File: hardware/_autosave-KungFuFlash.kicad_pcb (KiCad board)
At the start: 2 copper layers, 62 x 83.6 mm, 46 parts, among them J1 USB Power, J2 USB_B_Mini, J4 SWD, Q1 BC817, SW1 Reset, SW2 Menu, SW3 Special, U1 C64-Exp-Port, U2 AMS1117-3.3, U3 STM32F405RGTx, Y1 8MHz

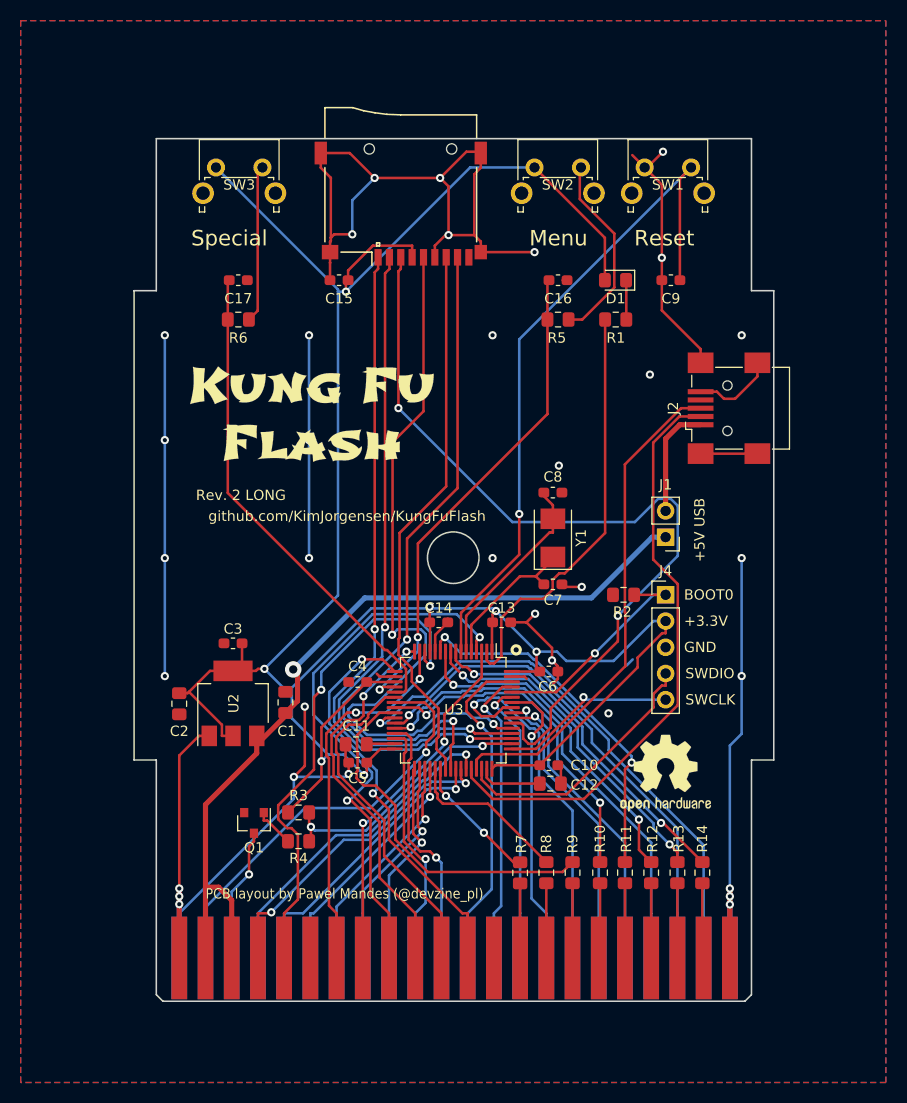
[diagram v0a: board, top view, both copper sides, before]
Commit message: Project migrated to KiCad 6.0
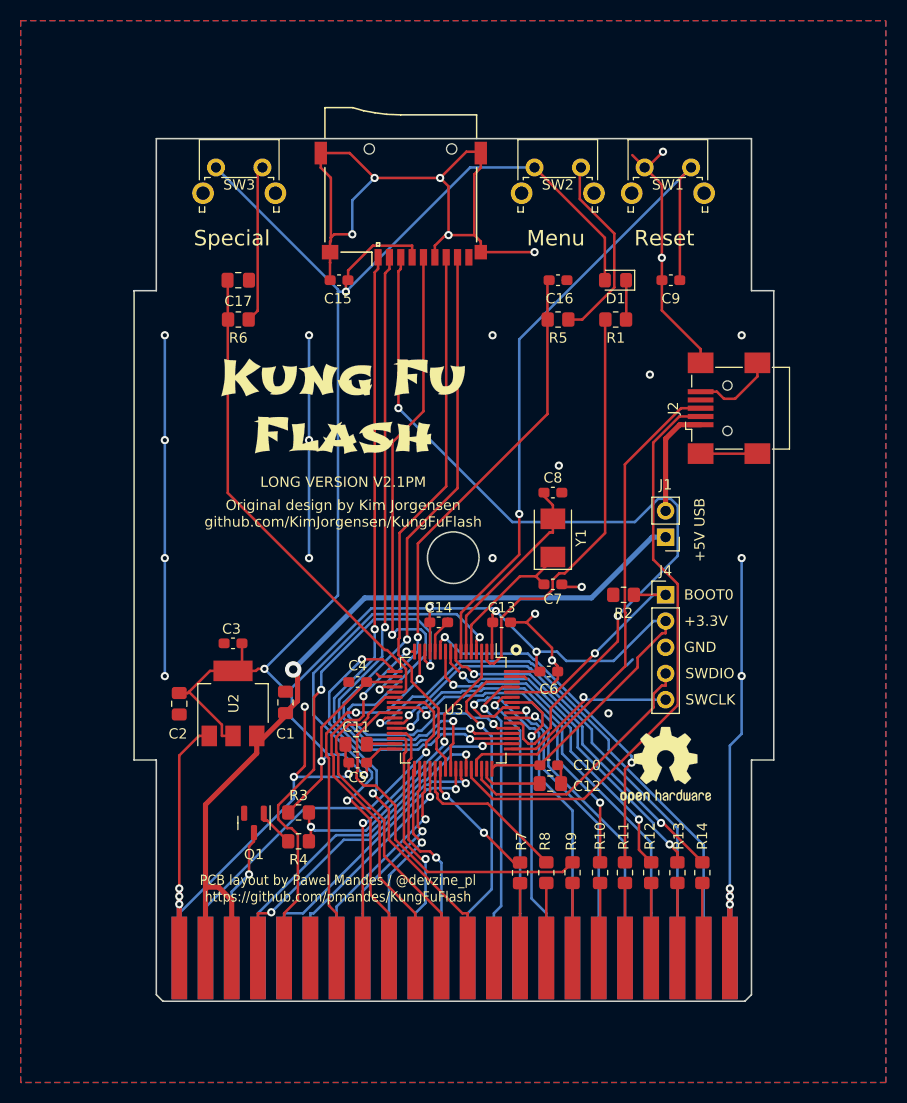
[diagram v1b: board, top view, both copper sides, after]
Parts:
- C1, C11, C12, C2: footprint Capacitor_SMD:C_0805_2012Metric_Pad1.15x1.40mm_HandSolder -> Capacitor_SMD:C_0805_2012Metric_Pad1.18x1.45mm_HandSolder
- C10, C13, C14, C15, C16, C3, C4, C5, C6, C7, C8, C9: footprint Capacitor_SMD:C_0603_1608Metric_Pad1.05x0.95mm_HandSolder -> Capacitor_SMD:C_0603_1608Metric_Pad1.08x0.95mm_HandSolder
- C17: footprint Capacitor_SMD:C_0603_1608Metric_Pad1.05x0.95mm_HandSolder -> Capacitor_SMD:C_0805_2012Metric_Pad1.18x1.45mm_HandSolder
- R1, R10, R11, R12, R13, R14, R2, R3, R4, R5, R6, R7, R8, R9: footprint Resistor_SMD:R_0805_2012Metric_Pad1.15x1.40mm_HandSolder -> Resistor_SMD:R_0805_2012Metric_Pad1.20x1.40mm_HandSolder
- moved G*** 3.12 mm to (89.7, 82.2)
- moved REF** 0.76 mm to (121.0, 117.0)
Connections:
- net /R~W renamed /R~{W}
- net /~EXROM renamed /~{EXROM}
- net /~GAME renamed /~{GAME}
- net /~IO1 renamed /~{IO1}
- net /~IO2 renamed /~{IO2}
- net /~IRQ renamed /~{IRQ}
- net /~LED renamed /~{LED}
- net /~NMI renamed /~{NMI}
- net /~RESET renamed /~{RESET}
- net /~ROMH renamed /~{ROMH}
- net /~ROML renamed /~{ROML}
- net /~RST renamed /~{RST}
- net /~RST_O renamed /~{RST_O}
- J2 pad 4: (no net) -> unconnected-(J2-Pad4)
- U1 pad 13: (no net) -> unconnected-(U1-Pad13)
- U1 pad 6: (no net) -> unconnected-(U1-Pad6)
- XS1 pad 9: (no net) -> unconnected-(XS1-Pad9)
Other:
- net class Default removed
- net class power removed
- board text added: "LONG VERSION V2.1PM"
- board text added: "Original design by Kim Jorgensen github.com/KimJorgensen/KungFuFlash"
- board text added: "PCB layout by Pawel Mandes / @devzine_pl https://github.com/pmandes/KungFuFlash"
- board text removed: "PCB layout by Pawel Mandes (@devzine_pl)"
- board text removed: "Rev. 2 LONG"
- board text removed: "github.com/KimJorgensen/KungFuFlash"
